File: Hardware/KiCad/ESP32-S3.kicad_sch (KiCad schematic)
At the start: 1 part, among them U1 ESP32-S3-WROOM-1

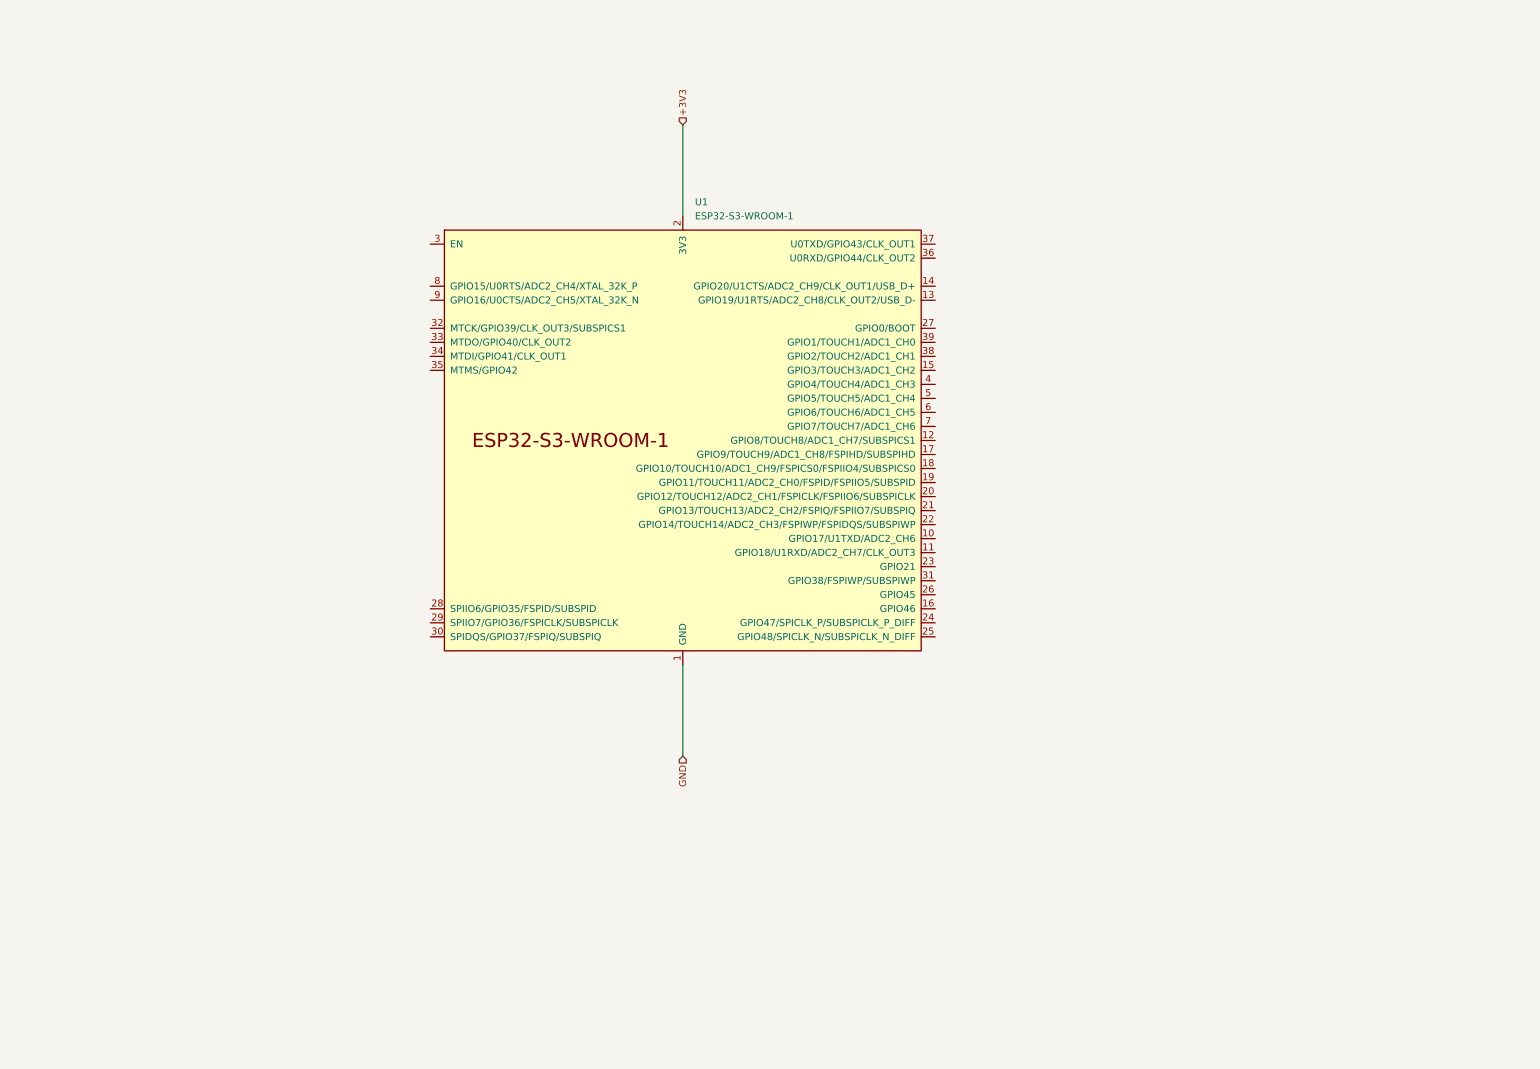
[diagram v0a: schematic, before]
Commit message: Add USB-C and Buttons to the Schematics, PCB and BOM
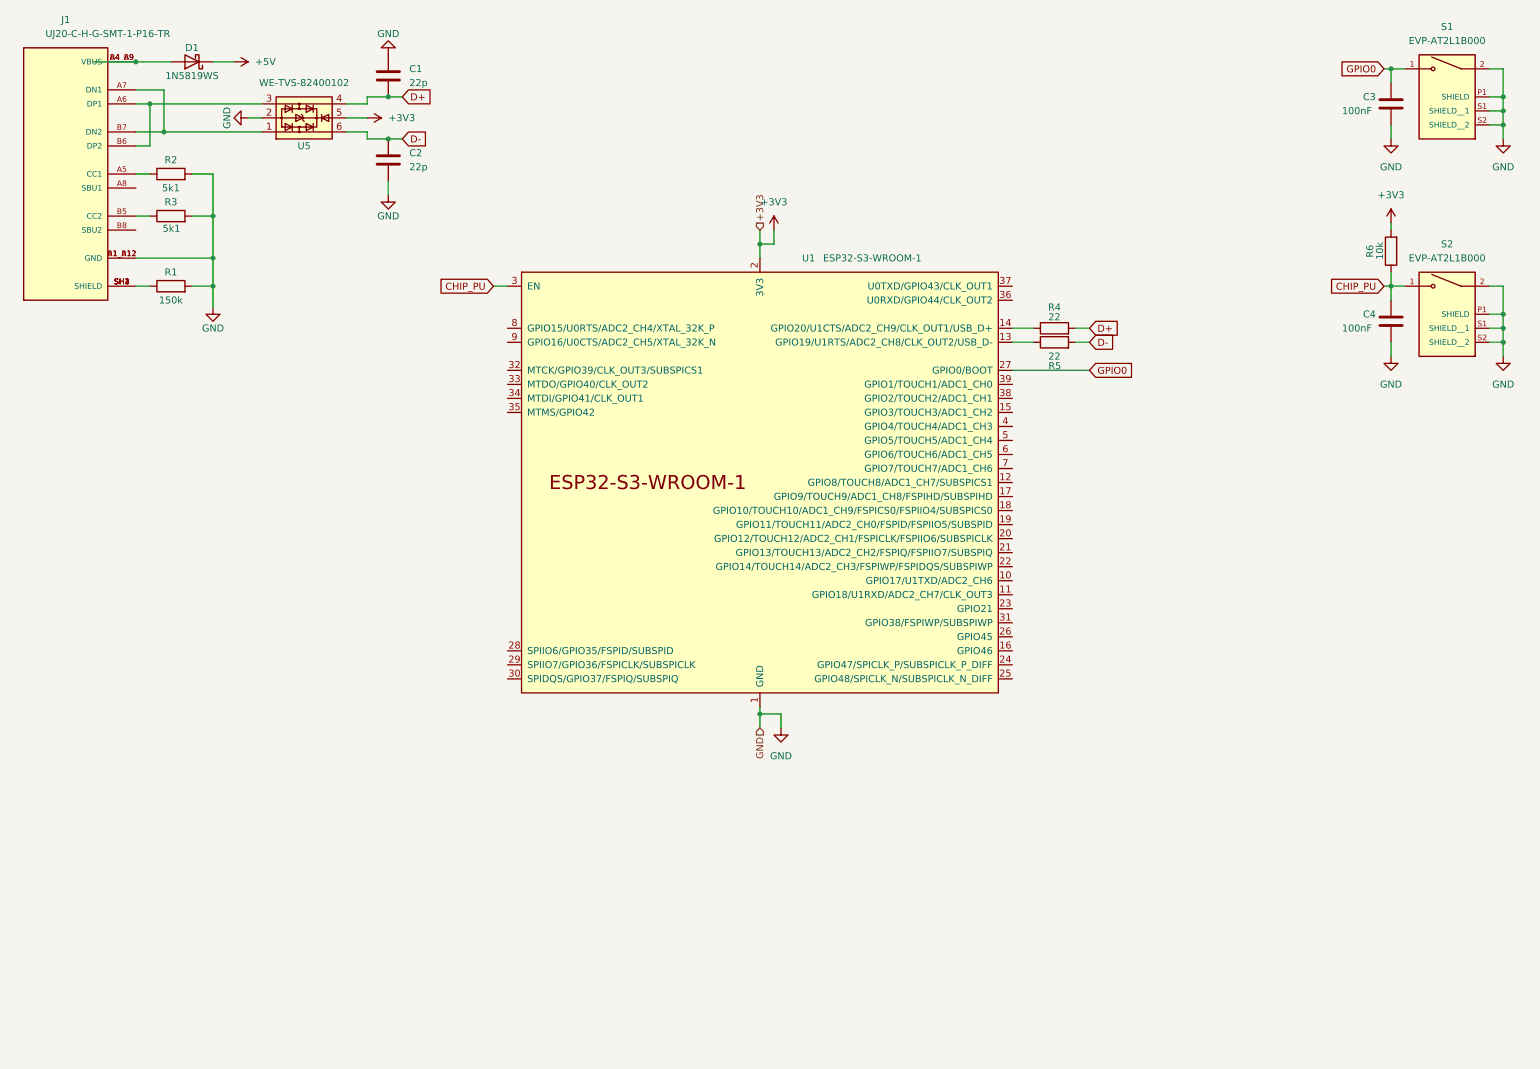
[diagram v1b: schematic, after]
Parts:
- added C1, C2: 22p, Capacitor_SMD:C_0603_1608Metric, symbol Device:C
- added C3, C4: 100nF, Capacitor_SMD:C_0603_1608Metric, symbol Device:C
- added D1: 1N5819WS, Diode_SMD:D_SOD-323, symbol Diode:1N5819WS
- added J1: UJ20-C-H-G-SMT-1-P16-TR, BugWiper_lib:SAMESKY_UJ20-C-H-G-SMT-1-P16-TR, symbol BugWiper_Lib:UJ20-C-H-G-SMT-1-P16-TR
- added R1: 150k, Resistor_SMD:R_0603_1608Metric, symbol Device:R
- added R2, R3: 5k1, Resistor_SMD:R_0603_1608Metric, symbol Device:R
- added R4, R5: 22, Resistor_SMD:R_0603_1608Metric, symbol Device:R
- added R6: 10k, Resistor_SMD:R_0603_1608Metric, symbol Device:R
- added S1, S2: EVP-AT2L1B000, BugWiper_lib:SW_EVP-AT2L1B000, symbol BugWiper_Lib:EVP-AT2L1B000
- added U5: WE-TVS-82400102, Package_TO_SOT_SMD:SOT-23-6, symbol Power_Protection:WE-TVS-82400102
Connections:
- net +3V3: now also R6.2, U5.5
- net GND: now also C1.1, C2.2, C3.2, C4.2, J1.A1_B12 (GND), J1.B1_A12 (GND), R1.2, R2.2, R3.2, S1.2, S1.P1 (SHIELD), S1.S1 (SHIELD__1), S1.S2 (SHIELD__2), S2.2, S2.P1 (SHIELD), S2.S1 (SHIELD__1), S2.S2 (SHIELD__2), U5.2
- net at U1.13 (GPIO19/U1RTS/ADC2_CH8/CLK_OUT2/USB_D-): now also R5.1
- net at U1.14 (GPIO20/U1CTS/ADC2_CH9/CLK_OUT1/USB_D+): now also R4.1
- net GPIO0: now reaches U1.27 (GPIO0/BOOT)
- net GPIO0: now also C3.1, S1.1
- net CHIP_PU: now reaches U1.3 (EN)
- net CHIP_PU: now also C4.1, R6.1, S2.1
- new net: J1.B5 (CC2), R3.1
- new net: D1.2 (A), J1.A4_B9 (VBUS), J1.B4_A9 (VBUS)
- new net: J1.A5 (CC1), R2.1
- new net: J1.A6 (DP1), J1.B6 (DP2), U5.3
- new net: J1.A7 (DN1), J1.B7 (DN2), U5.1
- new net: J1.SH1 (SHIELD), J1.SH2 (SHIELD), J1.SH3 (SHIELD), J1.SH4 (SHIELD), R1.1
- new net +5V: D1.1 (K)
- new net D+: C1.2, R4.2, U5.4
- new net D-: C2.1, R5.2, U5.6
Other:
- moved on the sheet: U1

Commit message: update KiCAD files
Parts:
- added R22, R23, R24: 1k, Resistor_SMD:R_0603_1608Metric, symbol Device:R
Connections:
- new net ADC_VBat: R24.2
- new net Encoder_C1: R22.2
- new net Encoder_C2: R23.2
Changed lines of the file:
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@@
+    (stroke (width 0) (type default))
+  )
+  (wire (pts (xy 245.11 146.05) (xy 248.92 146.05))
     (stroke (width 0) (type default))
   )
@@
     (stroke (width 0) (type default))
   )
+  (wire (pts (xy 245.11 132.08) (xy 248.92 132.08))
+    (stroke (width 0) (type default))
+  )
   (wire (pts (xy 261.62 33.02) (xy 261.62 35.56))
     (stroke (width 0) (type default))
@@
   )
   (wire (pts (xy 261.62 72.39) (xy 261.62 74.93))
+    (stroke (width 0) (type default))
+  )
+  (wire (pts (xy 245.11 138.43) (xy 248.92 138.43))
     (stroke (width 0) (type default))
   )
@@
     )
   )
+  (hierarchical_label "Encoder_C2" (shape input) (at 248.92 146.05 0) (fields_autoplaced)
+    (effects (font (size 1.27 1.27)) (justify left))
+  )
   (hierarchical_label "+3V3" (shape input) (at 147.32 52.07 90) (fields_autoplaced)
+    (effects (font (size 1.27 1.27)) (justify left))
+  )
+  (hierarchical_label "M_INH1" (shape input) (at 247.65 114.3 0) (fields_autoplaced)
     (effects (font (size 1.27 1.27)) (justify left))
   )
   (hierarchical_label "GND" (shape input) (at 147.32 142.24 270) (fields_autoplaced)
     (effects (font (size 1.27 1.27)) (justify right))
+  )
+  (hierarchical_label "ADC_VBat" (shape input) (at 248.92 132.08 0) (fields_autoplaced)
+    (effects (font (size 1.27 1.27)) (justify left))
+  )
+  (hierarchical_label "Encoder_C1" (shape input) (at 248.92 138.43 0) (fields_autoplaced)
+    (effects (font (size 1.27 1.27)) (justify left))
+  )
+  (hierarchical_label "M_IN1" (shape input) (at 247.65 107.95 0) (fields_autoplaced)
+    (effects (font (size 1.27 1.27)) (justify left))
+  )
+  (hierarchical_label "M_IS1" (shape input) (at 248.92 124.46 0) (fields_autoplaced)
+    (effects (font (size 1.27 1.27)) (justify left))
+  )
+  (hierarchical_label "M_IS2" (shape input) (at 248.92 128.27 0) (fields_autoplaced)
+    (effects (font (size 1.27 1.27)) (justify left))
+  )
+  (hierarchical_label "M_IHN2" (shape input) (at 247.65 116.84 0) (fields_autoplaced)
+    (effects (font (size 1.27 1.27)) (justify left))
+  )
+  (hierarchical_label "M_IN2" (shape input) (at 247.65 110.49 0) (fields_autoplaced)
+    (effects (font (size 1.27 1.27)) (justify left))
   )
   (symbol (lib_id "power:GND") (at 281.94 35.56 0) (unit 1)
@@
     )
   )
+  (symbol (lib_id "Device:R") (at 241.3 138.43 90) (unit 1)
+    (in_bom yes) (on_board yes) (dnp no)
+    (property "Reference" "R22" (at 241.3 134.62 90)
+      (effects (font (size 1.27 1.27)))
+    )
+    (property "Value" "1k" (at 241.2983 136.395 90)
+      (effects (font (size 1.27 1.27)))
+    )
+    (property "Footprint" "Resistor_SMD:R_0603_1608Metric" (at 241.3 140.208 90)
+      (effects (font (size 1.27 1.27)) hide)
+    )
+    (property "Datasheet" "~" (at 241.3 138.43 0)
+      (effects (font (size 1.27 1.27)) hide)
+    )
+    (pin "2")
+    (pin "1")
+    (instances
+      (project "BugWiperPCB"
+        (path "/d31a15bd-db02-4d4c-9593-17c596d3182c/caaad550-b4dc-4462-8f3c-cac307d6a6e2"
+          (reference "R22") (unit 1)
+        )
+      )
+    )
+  )
   (symbol (lib_id "power:GND") (at 261.62 35.56 0) (unit 1)
     (in_bom yes) (on_board yes) (dnp no)
@@
     )
   )
+  (symbol (lib_id "Device:R") (at 241.3 146.05 90) (unit 1)
+    (in_bom yes) (on_board yes) (dnp no)
+    (property "Reference" "R23" (at 241.3 142.24 90)
+      (effects (font (size 1.27 1.27)))
+    )
+    (property "Value" "1k" (at 241.2983 144.015 90)
+      (effects (font (size 1.27 1.27)))
+    )
+    (property "Footprint" "Resistor_SMD:R_0603_1608Metric" (at 241.3 147.828 90)
+      (effects (font (size 1.27 1.27)) hide)
+    )
+    (property "Datasheet" "~" (at 241.3 146.05 0)
+      (effects (font (size 1.27 1.27)) hide)
+    )
+    (pin "2")
+    (pin "1")
+    (instances
+      (project "BugWiperPCB"
+        (path "/d31a15bd-db02-4d4c-9593-17c596d3182c/caaad550-b4dc-4462-8f3c-cac307d6a6e2"
+          (reference "R23") (unit 1)
+        )
+      )
+    )
+  )
   (symbol (lib_id "power:GND") (at 281.94 74.93 0) (unit 1)
     (in_bom yes) (on_board yes) (dnp no) (fields_autoplaced)
@@
         )
       )
+    )
+  )
+  (symbol (lib_id "Device:R") (at 241.3 132.08 90) (unit 1)
+    (in_bom yes) (on_board yes) (dnp no)
+    (property "Reference" "R24" (at 241.3 128.27 90)
+      (effects (font (size 1.27 1.27)))
+    )
+    (property "Value" "1k" (at 241.2983 130.045 90)
+      (effects (font (size 1.27 1.27)))
+    )
+    (property "Footprint" "Resistor_SMD:R_0603_1608Metric" (at 241.3 133.858 90)
+      (effects (font (size 1.27 1.27)) hide)
+    )
+    (property "Datasheet" "~" (at 241.3 132.08 0)
+      (effects (font (size 1.27 1.27)) hide)
+    )
+    (pin "2")
+    (pin "1")
+    (instances
+      (project "BugWiperPCB"
+        (path "/d31a15bd-db02-4d4c-9593-17c596d3182c/caaad550-b4dc-4462-8f3c-cac307d6a6e2"
+          (reference "R24") (unit 1)
+        )
+      )

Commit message: Update PCB
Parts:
- added J4: RJ45, BugWiper_lib:CONN8_2-908LF_AMP, symbol Connector:RJ45
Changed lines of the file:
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@@
+    )
+  )
+  (symbol (lib_id "Connector:RJ45") (at 27.94 167.64 0) (unit 1)
+    (in_bom yes) (on_board yes) (dnp no) (fields_autoplaced)
+    (property "Reference" "J4" (at 27.94 149.86 0)
+      (effects (font (size 1.27 1.27)))
+    )
+    (property "Value" "RJ45" (at 27.94 152.4 0)
+      (effects (font (size 1.27 1.27)))
+    )
+    (property "Footprint" "BugWiper_lib:CONN8_2-908LF_AMP" (at 27.94 167.005 90)
+      (effects (font (size 1.27 1.27)) hide)
+    )
+    (property "Datasheet" "~" (at 27.94 167.005 90)
+      (effects (font (size 1.27 1.27)) hide)
+    )
+    (pin "7")
+    (pin "6")
+    (pin "4")
+    (pin "5")
+    (pin "2")
+    (pin "1")
+    (pin "3")
+    (pin "8")
+    (instances
+      (project "BugWiperPCB"
+        (path "/d31a15bd-db02-4d4c-9593-17c596d3182c/caaad550-b4dc-4462-8f3c-cac307d6a6e2"
+          (reference "J4") (unit 1)
+        )
+      )
     )
   )

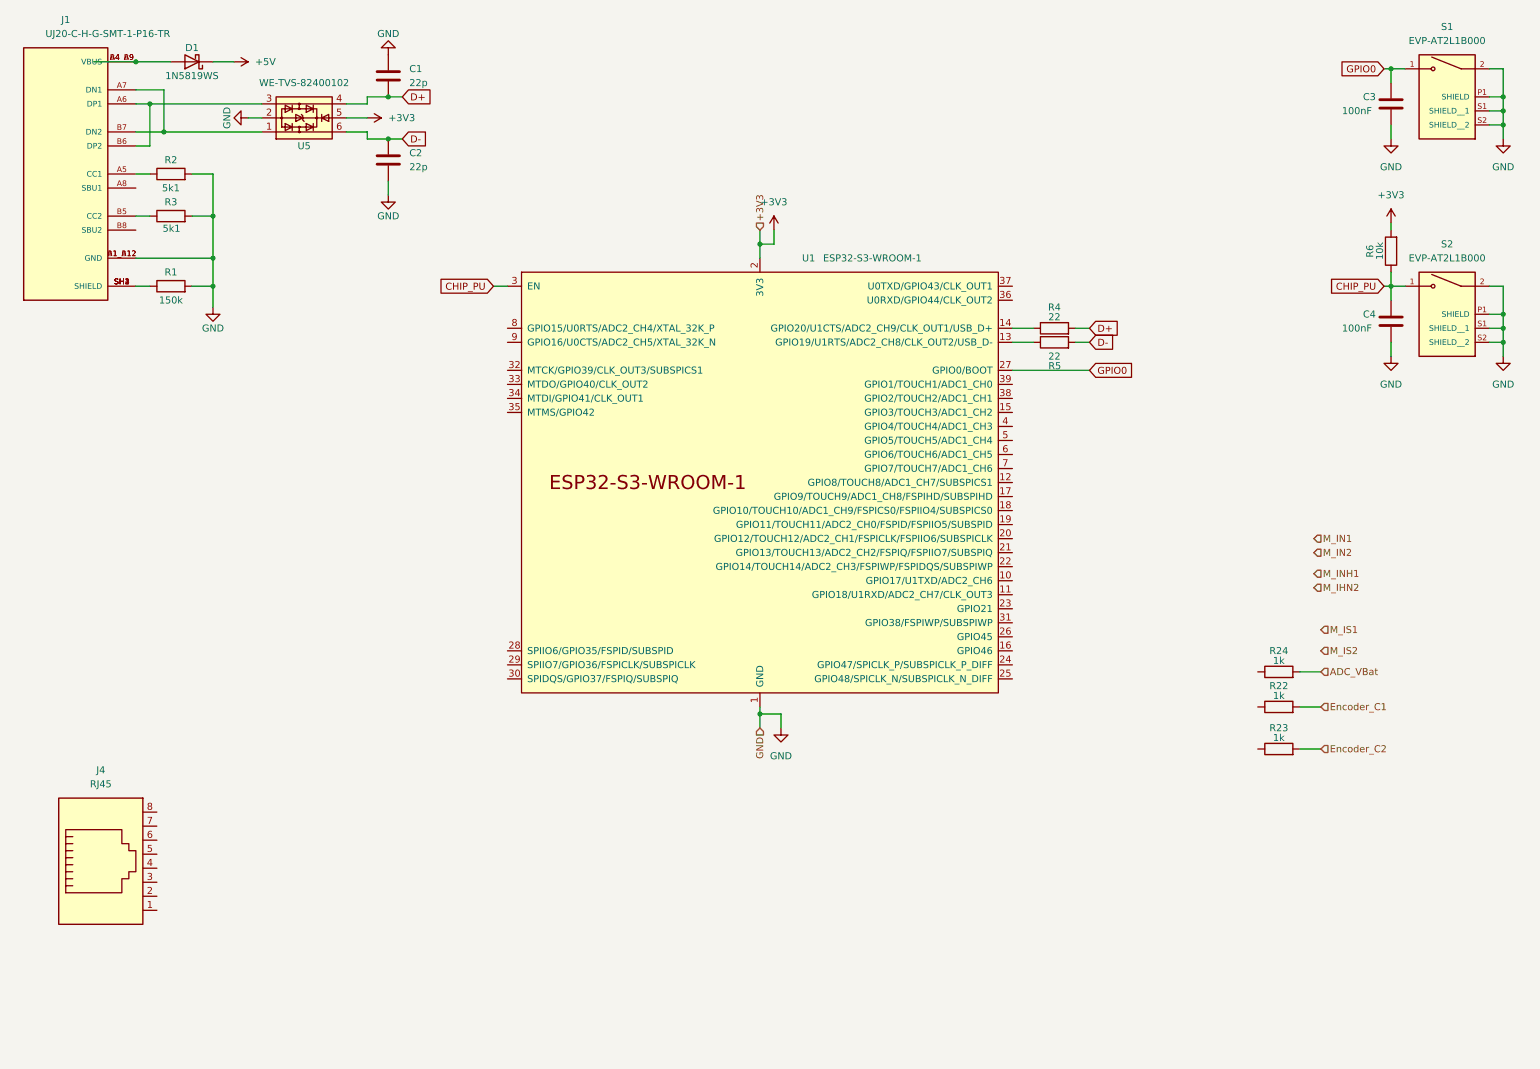
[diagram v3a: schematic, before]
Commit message: update PCB
add 12V to 3.3V converter and 5V to 3.3V for USB
add protections to the RJ45
component placement
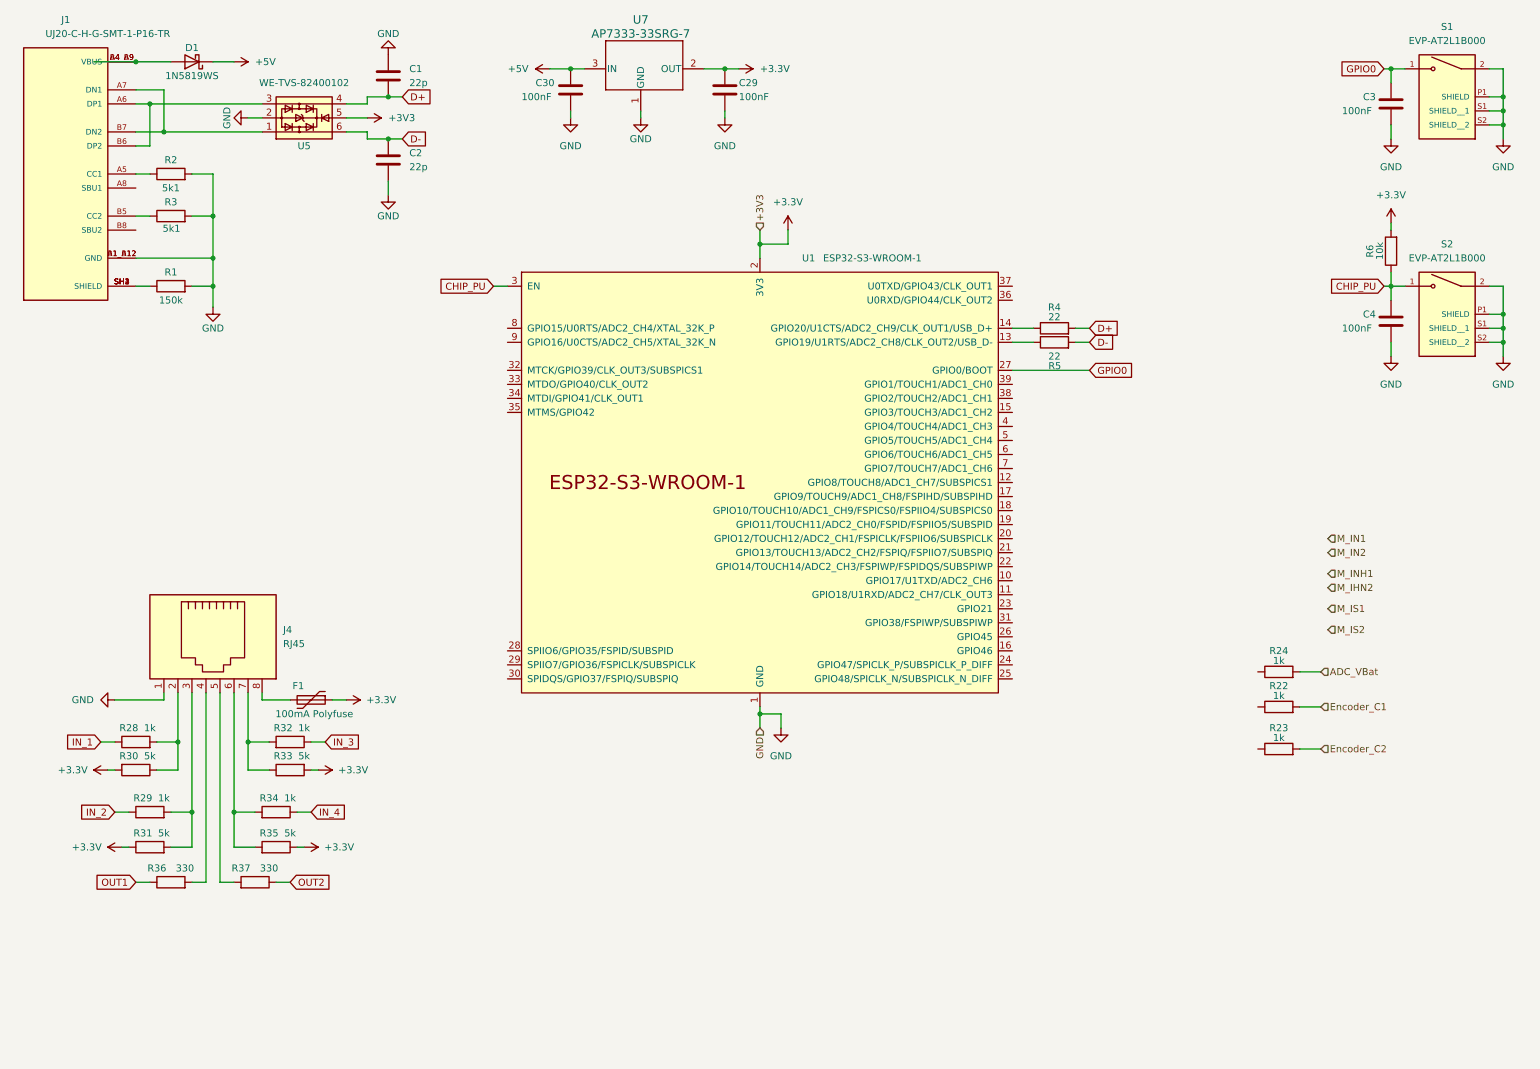
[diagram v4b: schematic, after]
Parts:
- added C29, C30: 100nF, Capacitor_SMD:C_0603_1608Metric, symbol Device:C
- added F1: 100mA Polyfuse, Resistor_SMD:R_1206_3216Metric, symbol Device:Polyfuse
- added R28, R29, R32, R34: 1k, Resistor_SMD:R_0603_1608Metric, symbol Device:R
- added R30, R31, R33, R35: 5k, Resistor_SMD:R_0603_1608Metric, symbol Device:R
- added R36, R37: 330, Resistor_SMD:R_0603_1608Metric, symbol Device:R
- added U7: AP7333-33SRG-7, SOT23R_DIO, symbol BugWiper_Lib:AP7333-33SRG-7
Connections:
- net +5V: now also C30.1, U7.3 (IN)
- net GND: now also J4.1, C29.2, C30.2, U7.1 (GND)
- net at J4.2: now also R28.2, R30.1
- net at J4.3: now also R29.2, R31.2
- net at J4.4: now also R36.2
- net at J4.5: now also R37.2
- net at J4.6: now also R34.2, R35.2
- net at J4.7: now also R32.2, R33.1
- net at J4.8: now also F1.2
- net +3V3 renamed +3.3V
- net +3.3V: now also C29.1, F1.1, R30.2, R31.1, R33.2, R35.1, U7.2 (OUT)
- new net IN_1: R28.1
- new net IN_2: R29.1
- new net IN_3: R32.1
- new net IN_4: R34.1
- new net OUT1: R36.1
- new net OUT2: R37.1
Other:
- moved on the sheet: J4
